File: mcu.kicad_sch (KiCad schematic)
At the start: 2 parts, among them U1 STM32G0B0KETx

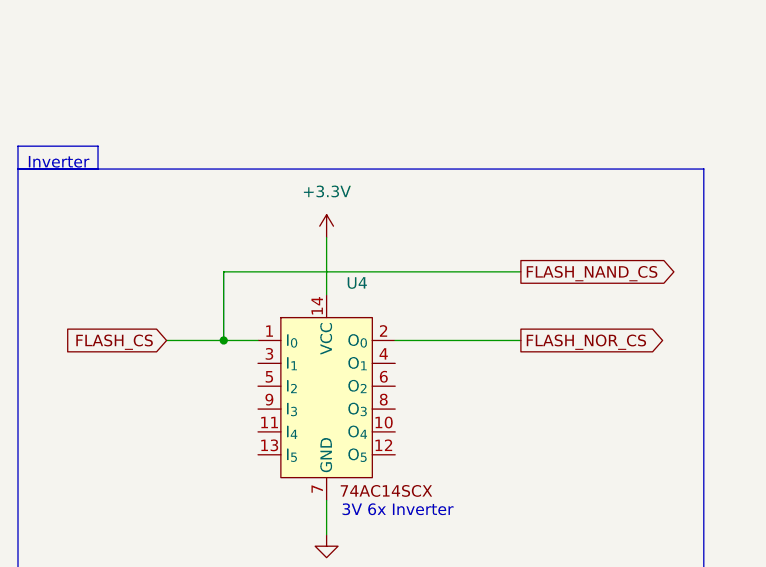
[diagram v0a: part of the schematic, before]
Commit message: added usbc power supply
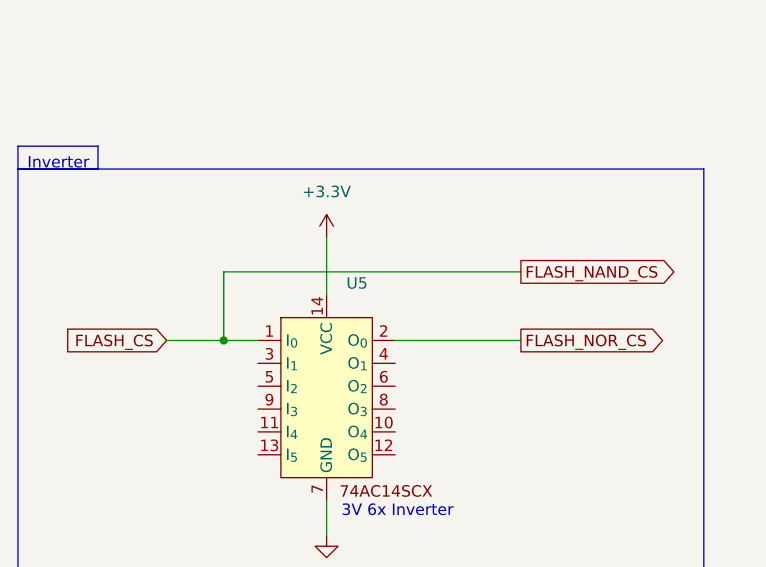
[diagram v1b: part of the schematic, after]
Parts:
- removed U4: ~, symbol custom:74AC14SCX
- added U5: ~, symbol custom:74AC14SCX (Inverter 6x)
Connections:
- net +3.3V: now also U5.14 (VCC)
- net FLASH_CS: now also U5.1 (I_{0})
- net FLASH_NOR_CS: now also U5.2 (O_{0})
- net GND: now also U5.7 (GND)
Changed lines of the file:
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@@
+	(wire
+		(pts
+			(xy 58.42 149.86) (xy 58.42 156.21)
+		)
+		(stroke
+			(width 0)
+			(type default)
+		)
+	)
+	(wire
+		(pts
+			(xy 58.42 179.07) (xy 58.42 182.88)
+		)
+		(stroke
+			(width 0)
+			(type default)
+		)
+	)
+	(wire
+		(pts
+			(xy 66.04 161.29) (xy 80.01 161.29)
+		)
+		(stroke
+			(width 0)
+			(type default)
+		)
+	)
 	(wire
 		(pts
@@
 	(wire
 		(pts
-			(xy 58.42 179.07) (xy 58.42 182.88)
-		)
-		(stroke
-			(width 0)
-			(type default)
-		)
-	)
-	(wire
-		(pts
-			(xy 58.42 149.86) (xy 58.42 156.21)
-		)
-		(stroke
-			(width 0)
-			(type default)
-		)
-	)
-	(wire
-		(pts
 			(xy 46.99 161.29) (xy 50.8 161.29)
 		)
@@
 		(pts
 			(xy 46.99 161.29) (xy 46.99 153.67)
-		)
-		(stroke
-			(width 0)
-			(type default)
-		)
-	)
-	(wire
-		(pts
-			(xy 66.04 161.29) (xy 80.01 161.29)
 		)
 		(stroke
@@
 				(justify left)
 				(hide yes)
+			)
+		)
+	)
+	(symbol
+		(lib_id "custom:74AC14SCX (Inverter 6x)")
+		(at 58.42 167.64 0)
+		(unit 1)
+		(exclude_from_sim no)
+		(in_bom yes)
+		(on_board yes)
+		(dnp no)
+		(fields_autoplaced yes)
+		(property "Reference" "U5"
+			(at 60.6141 154.94 0)
+			(effects
+				(font
+					(size 1.27 1.27)
+				)
+				(justify left)
+			)
+		)
+		(property "Value" "~"
+			(at 60.6141 157.48 0)
+			(effects
+				(font
+					(size 1.27 1.27)
+				)
+				(justify left)
+			)
+		)
+		(property "Footprint" ""
+			(at 58.42 167.64 0)
+			(effects
+				(font
+					(size 1.27 1.27)
+				)
+				(hide yes)
+			)
+		)
+		(property "Datasheet" ""
+			(at 58.42 167.64 0)
+			(effects
+				(font
+					(size 1.27 1.27)
+				)
+				(hide yes)
+			)
+		)
+		(property "Description" ""
+			(at 58.42 167.64 0)
+			(effects
+				(font
+					(size 1.27 1.27)
+				)
+				(hide yes)
+			)
+		)
+		(pin "2"
+		)
+		(pin "9"
+		)
+		(pin "6"
+		)
+		(pin "5"
+		)
+		(pin "1"
+		)
+		(pin "14"
+		)
+		(pin "4"
+		)
+		(pin "8"
+		)
+		(pin "11"
+		)
+		(pin "13"
+		)
+		(pin "12"
+		)
+		(pin "10"
+		)
+		(pin "3"
+		)
+		(pin "7"
+		)
+		(instances
+			(project ""
+				(path "/342e1e7c-839e-4cd3-a9c3-2caee679f2e5/a7559ae8-f430-4530-8ad5-dc150bb98484"
+					(reference "U5")
+					(unit 1)
+				)
 			)
 		)
@@
 					(unit 1)
 				)
-			)
-		)
-	)
-	(symbol
-		(lib_id "custom:74AC14SCX")
-		(at 58.42 167.64 0)
-		(unit 1)
-		(exclude_from_sim no)
-		(in_bom yes)
-		(on_board yes)
-		(dnp no)
-		(fields_autoplaced yes)
-		(property "Reference" "U4"
-			(at 60.6141 154.94 0)
-			(effects
-				(font
-					(size 1.27 1.27)
-				)
-				(justify left)
-			)
-		)
-		(property "Value" "~"
-			(at 60.6141 157.48 0)
-			(effects
-				(font
-					(size 1.27 1.27)
-				)
-				(justify left)
-			)
-		)
-		(property "Footprint" ""
-			(at 58.42 167.64 0)
-			(effects
-				(font
-					(size 1.27 1.27)
-				)
-				(hide yes)
-			)
-		)
-		(property "Datasheet" ""
-			(at 58.42 167.64 0)
-			(effects
-				(font
-					(size 1.27 1.27)
-				)
-				(hide yes)
-			)
-		)
-		(property "Description" ""
-			(at 58.42 167.64 0)
-			(effects
-				(font
-					(size 1.27 1.27)
-				)
-				(hide yes)
-			)
-		)
-		(pin "9"
-		)
-		(pin "7"
-		)
-		(pin "13"
-		)
-		(pin "2"
-		)
-		(pin "3"
-		)
-		(pin "12"
-		)
-		(pin "1"
-		)
-		(pin "10"
-		)
-		(pin "6"
-		)
-		(pin "8"
-		)
-		(pin "4"
-		)
-		(pin "5"
-		)
-		(pin "11"
-		)
-		(pin "14"
-		)
-		(instances
-			(project "stm32G0_mcu"
-				(path "/342e1e7c-839e-4cd3-a9c3-2caee679f2e5/a7559ae8-f430-4530-8ad5-dc150bb98484"
-					(reference "U4")
-					(unit 1)
-				)

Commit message: dasda
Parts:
- U5: footprint (none) -> custom:74AC14SCX
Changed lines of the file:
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@@
 			)
 		)
-		(property "Footprint" ""
+		(property "Footprint" "custom:74AC14SCX"
 			(at 58.42 167.64 0)
 			(effects
